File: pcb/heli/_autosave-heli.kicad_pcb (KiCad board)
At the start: 4 copper layers, 50.6 x 50 mm, 68 parts, among them J1 Batterie, J2 Debug, J4 Servo, J5 Servo, M1 Motor_DC, M2 Motor_DC, Q1 IRLZ44N, Q2 BC547, Q3 IRLZ44N, Q4 BC547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

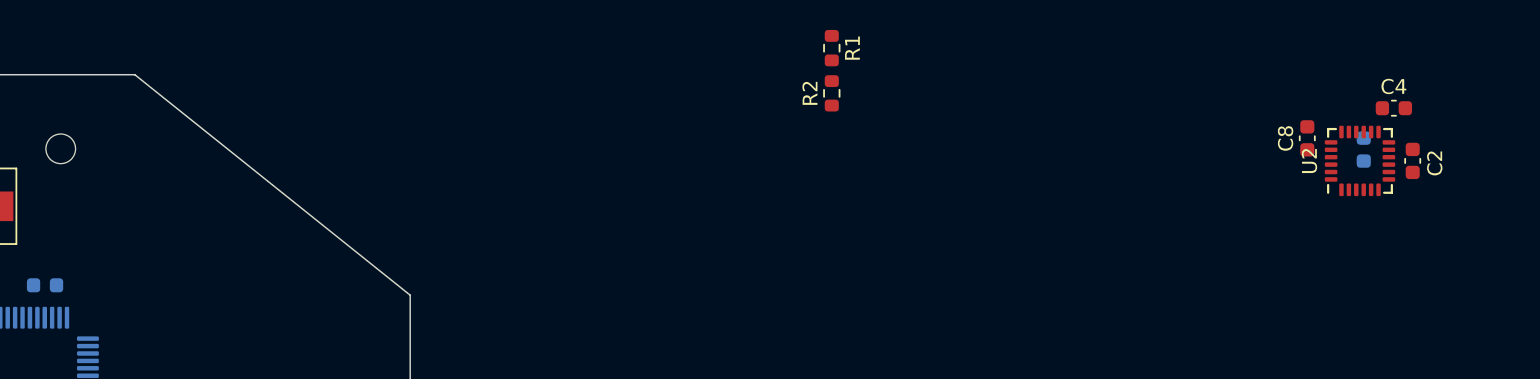
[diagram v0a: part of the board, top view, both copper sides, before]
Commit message: 
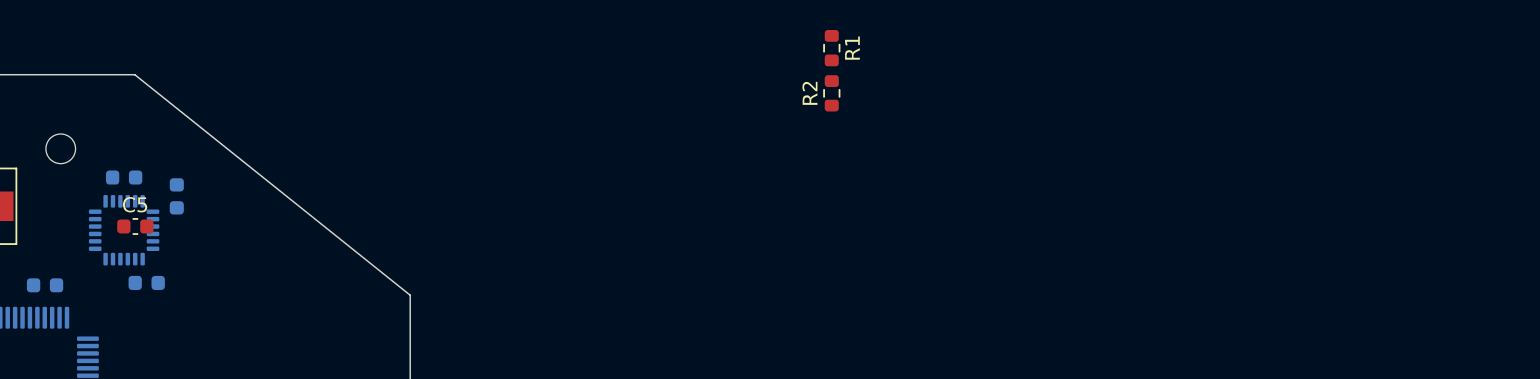
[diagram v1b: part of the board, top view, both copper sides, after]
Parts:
- C2, C4, C8, U2: moved to B.Cu
- C5: moved to F.Cu
- moved C2 87.0 mm to (49.3, 21.9), turned to 0 degrees
- moved U2 83.5 mm to (49.3, 25.5), turned to 0 degrees
- moved C5 83.0 mm to (50.0, 25.2), turned to 0 degrees
- moved C4 82.3 mm to (52.8, 23.2), turned to 90 degrees
- moved C8 78.9 mm to (50.8, 29.1), turned to 0 degrees
